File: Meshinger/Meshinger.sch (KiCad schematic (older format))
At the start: 0 parts

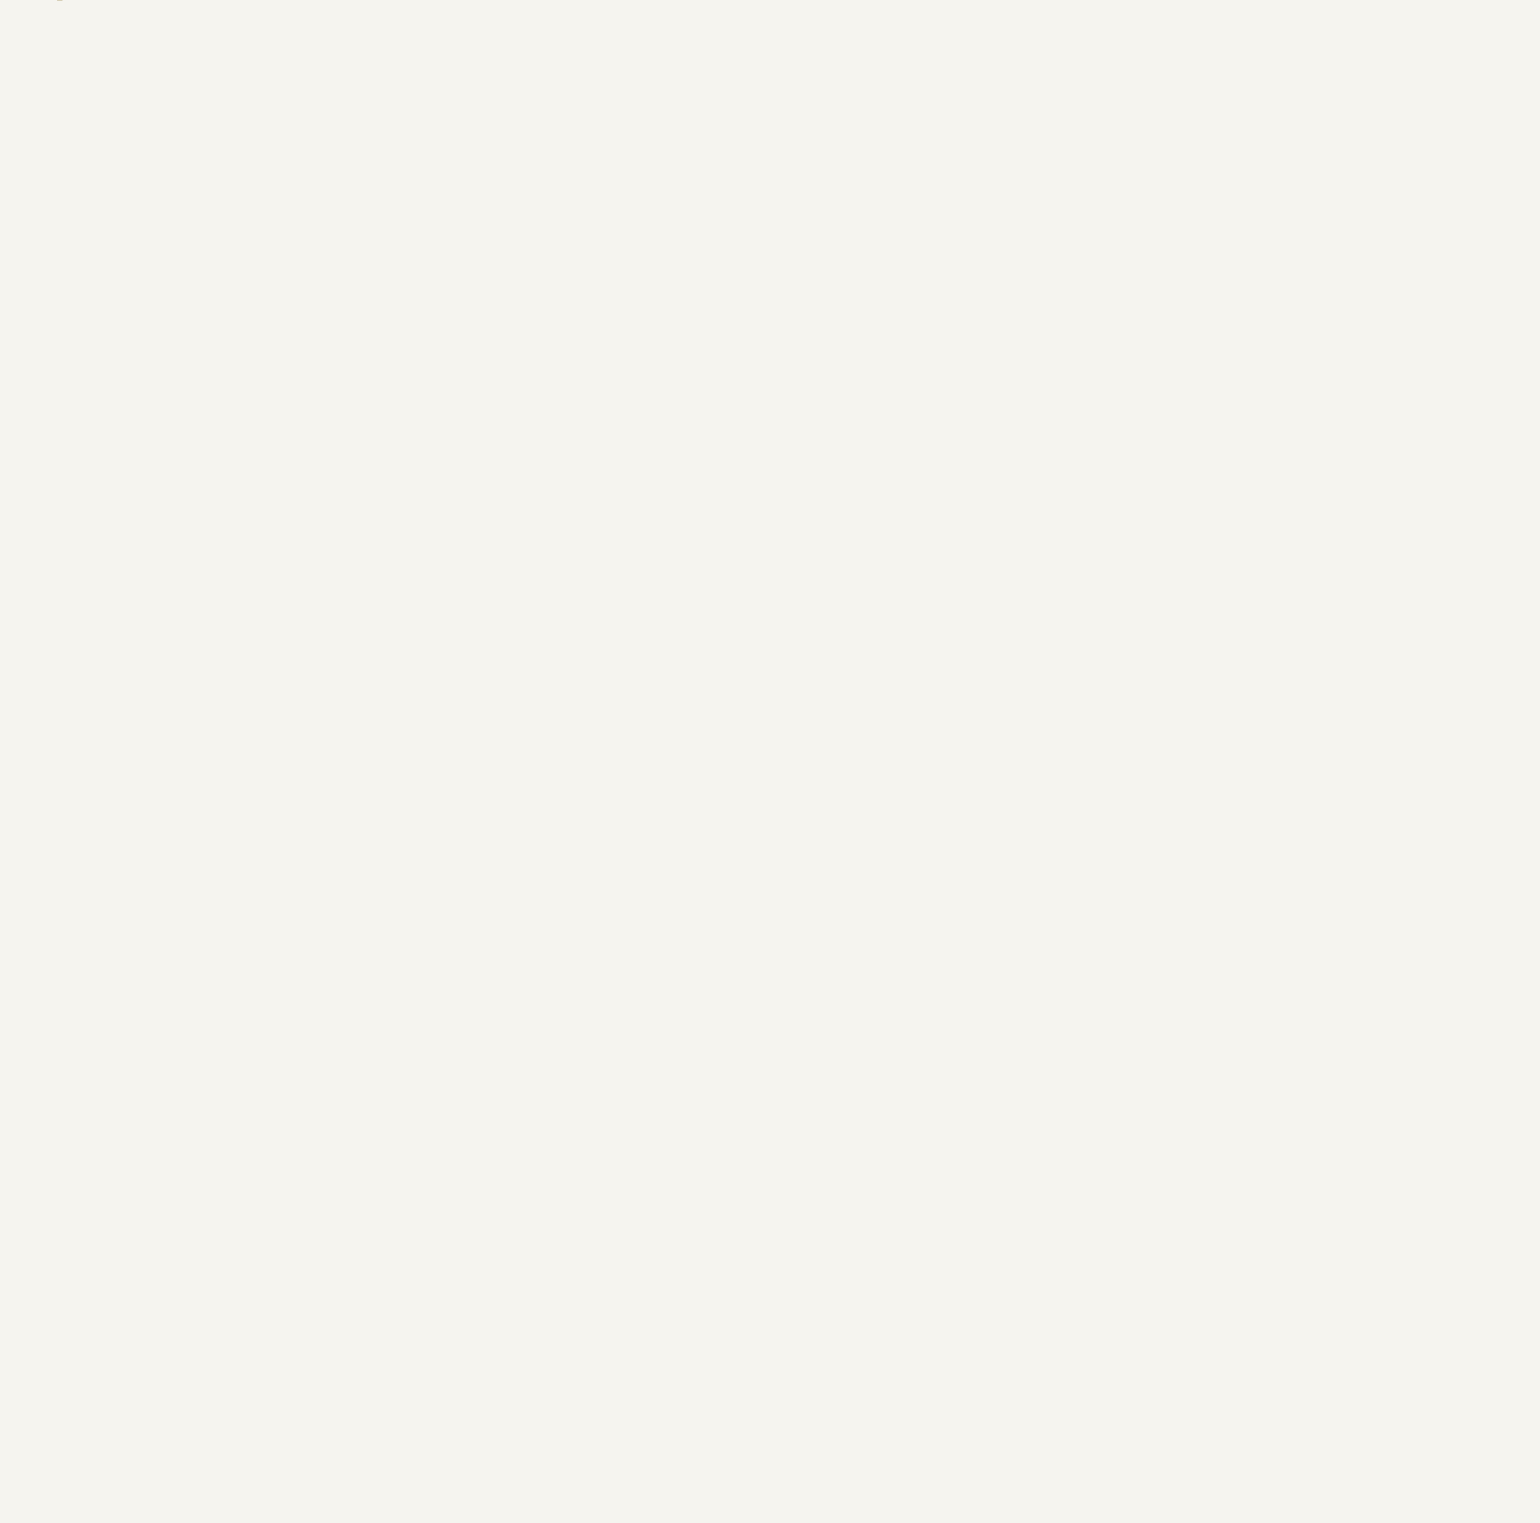
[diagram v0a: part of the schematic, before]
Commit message: Meshinger 1.0 rev B WARNING THE DC PLUG PINS ARE WRONG, SHORTS BATTERY!
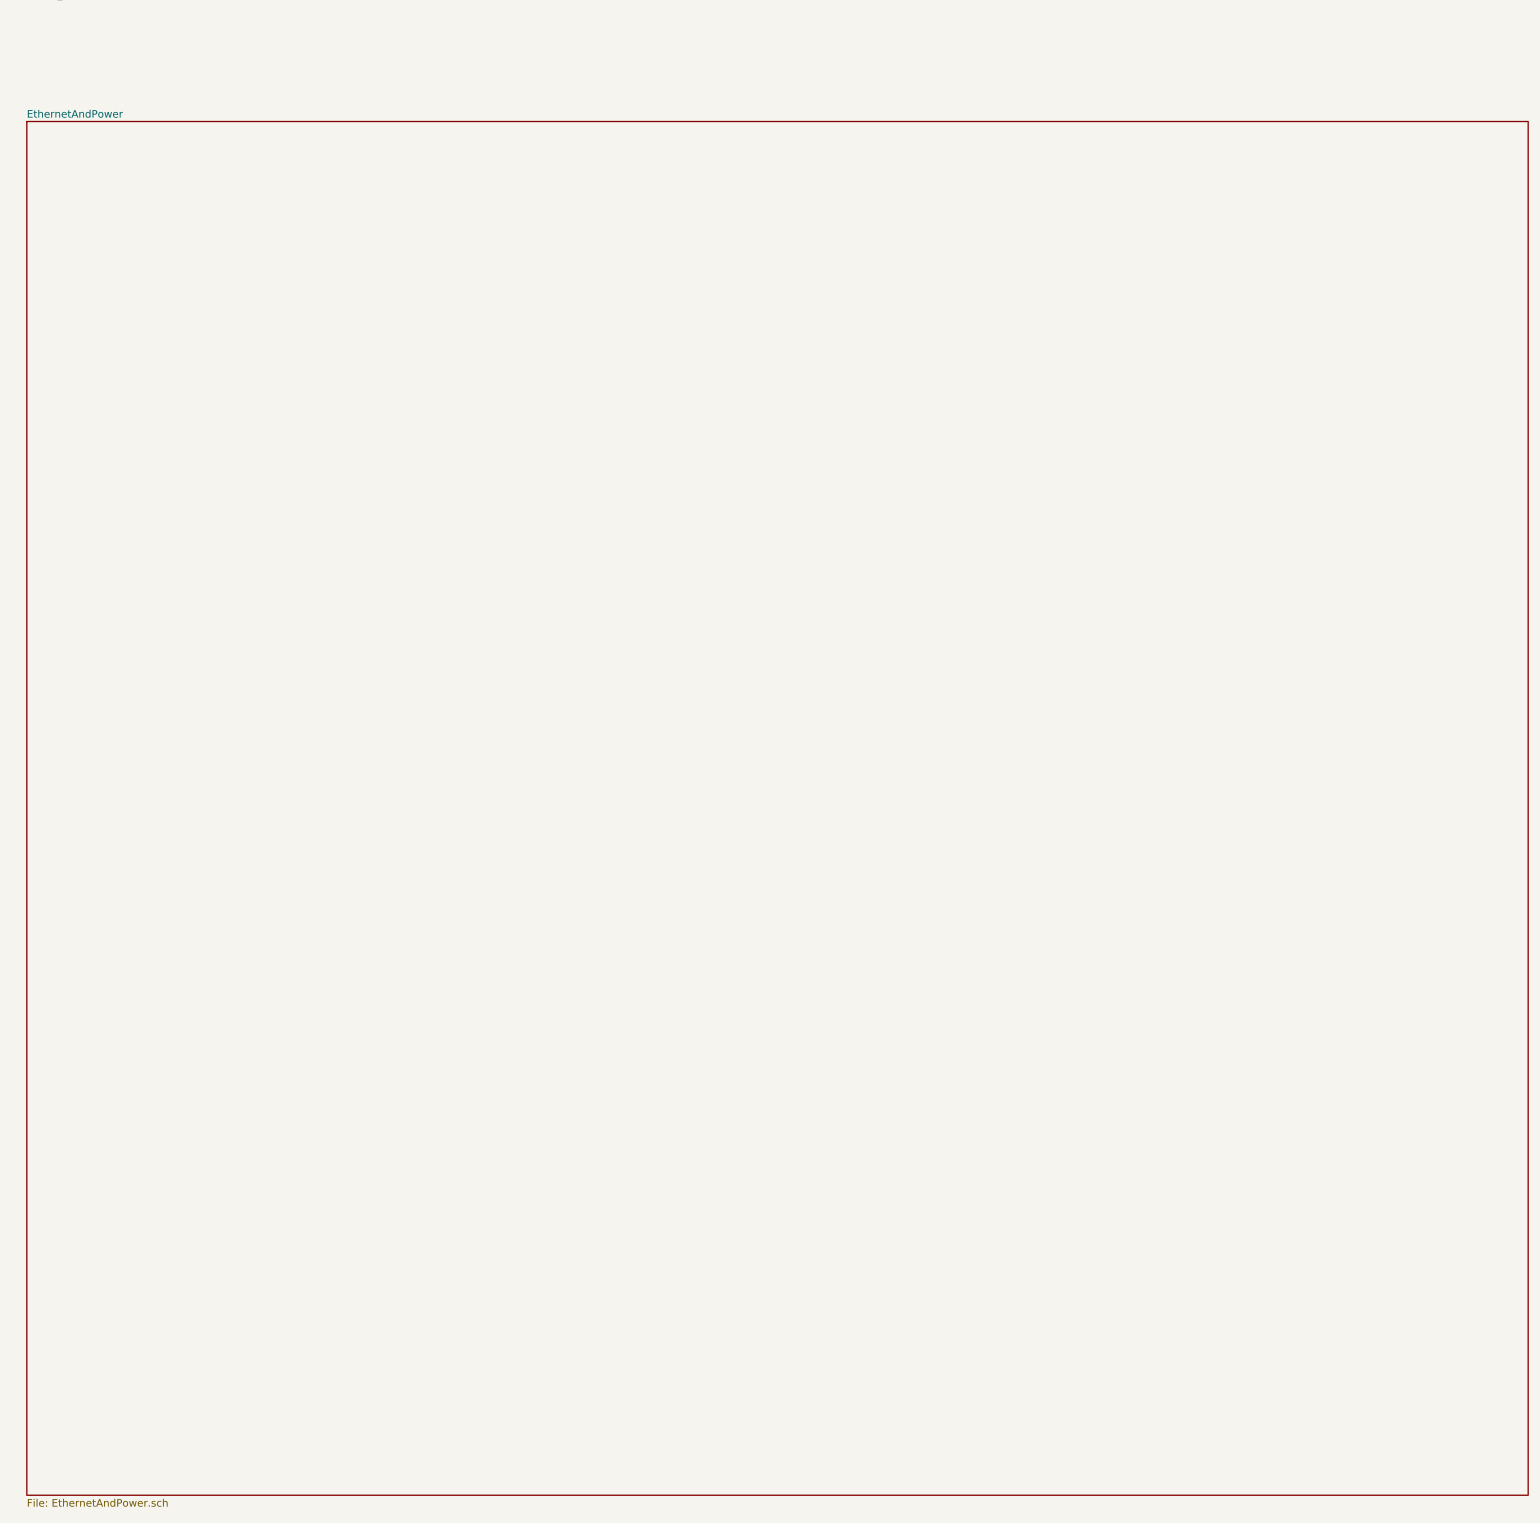
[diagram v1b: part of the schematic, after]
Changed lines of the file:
@@
 $Descr A4 11693 8268
 encoding utf-8
-Sheet 1 3
+Sheet 1 4
 Title ""
 Date ""
@@
 F1 "SkylabModule.sch" 50
 $EndSheet
+$Sheet
+S 13050 8950 10000 9150
+U 606A5CC1
+F0 "EthernetAndPower" 50
+F1 "EthernetAndPower.sch" 50
+$EndSheet
 $EndSCHEMATC
